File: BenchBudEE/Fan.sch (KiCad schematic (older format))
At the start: 11 parts, among them Q2 DMN65D8L-7, Q3 B130-13-F, Q4 B130-13-F, U10 MCP4801, U4 OPA4170

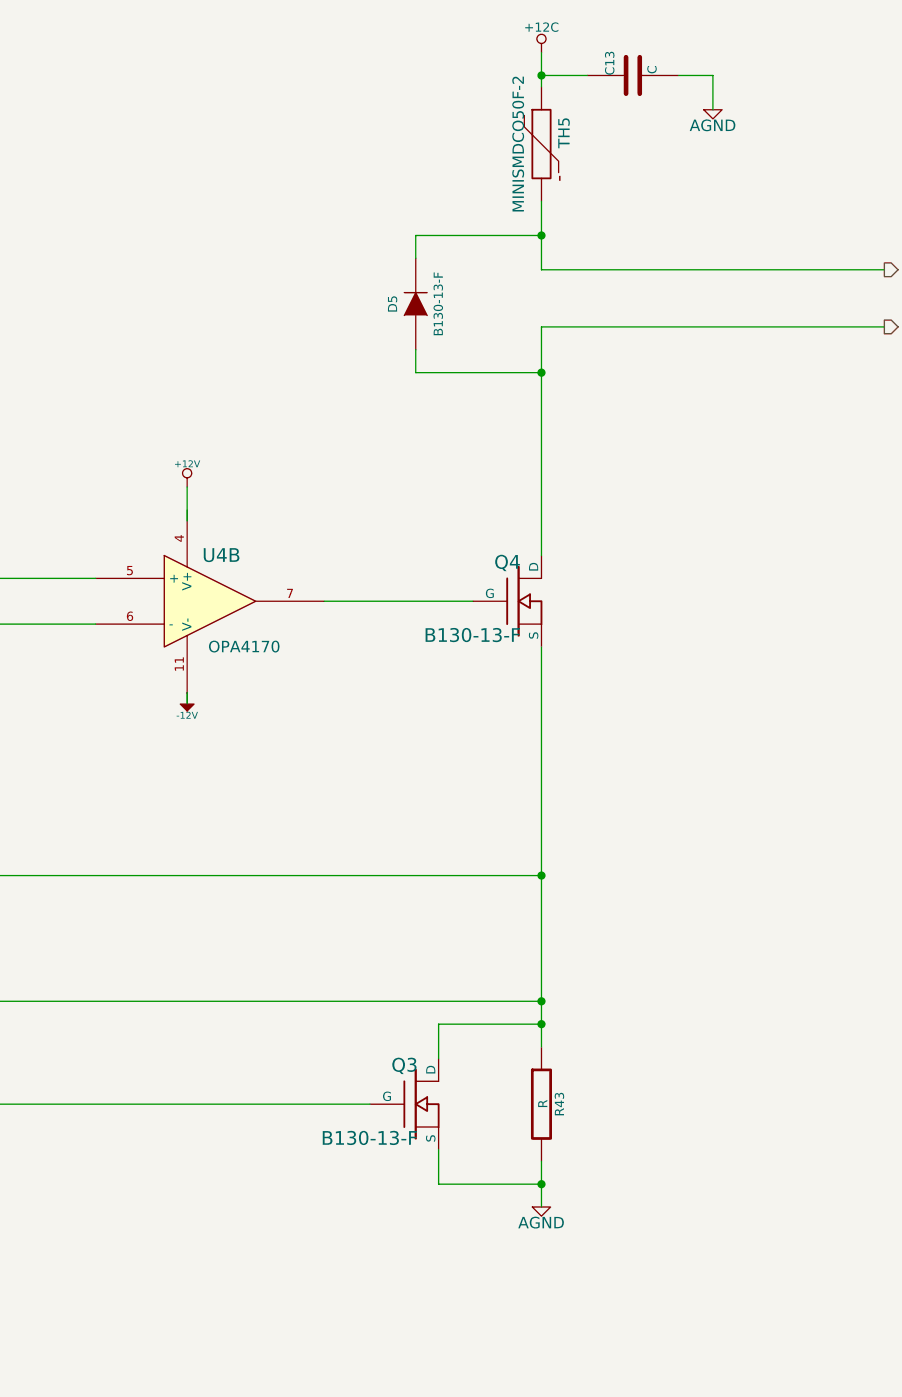
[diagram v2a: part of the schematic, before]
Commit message: Ground and Power Planes
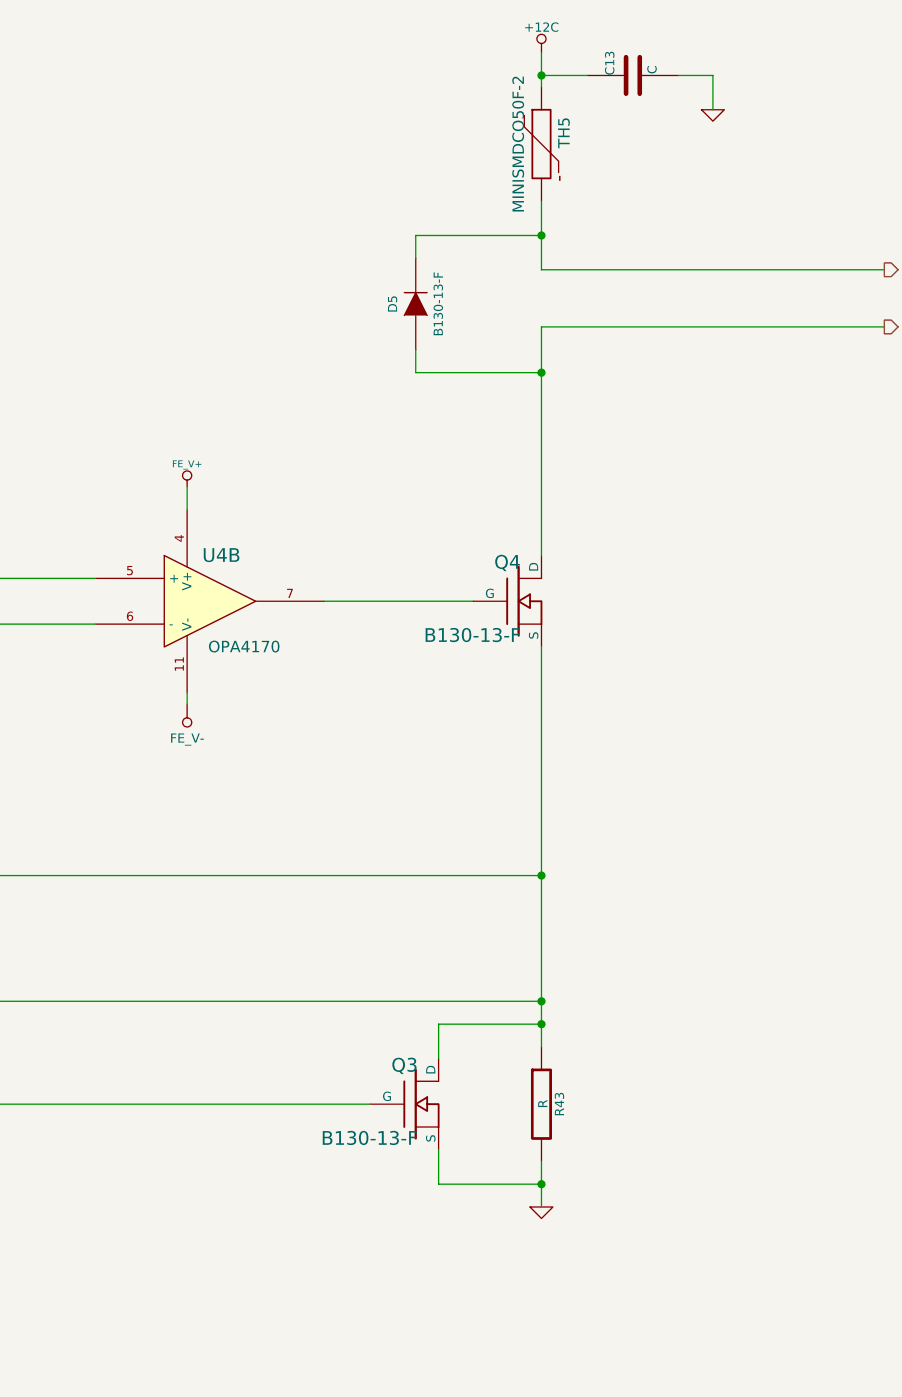
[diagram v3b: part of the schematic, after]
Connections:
- net labels added: FE_V+, FE_V-, GND
- net labels removed: +12V, -12V
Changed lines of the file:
@@
 Sheet 9 9
 Title ""
-Date "27 feb 2014"
+Date "1 mar 2014"
 Rev ""
 Comp ""
@@
 	1    0    0    -1
 $EndComp
-$Comp
-L AGND #PWR055
-U 1 1 52F13D75
-P 9100 5750
-F 0 "#PWR055" H 9100 5750 40  0001 C CNN
-F 1 "AGND" H 9100 5680 50  0000 C CNN
-F 2 "" H 9100 5750 60  0000 C CNN
-F 3 "" H 9100 5750 60  0000 C CNN
-	1    9100 5750
-	1    0    0    -1
-$EndComp
 Wire Wire Line
 	9100 5550 9100 5750
 Wire Wire Line
 	6100 3200 7150 3200
-$Comp
-L +12V #PWR056
-U 1 1 52F13D90
-P 7550 2600
-F 0 "#PWR056" H 7550 2550 20  0001 C CNN
-F 1 "+12V" H 7550 2700 30  0000 C CNN
-F 2 "" H 7550 2600 60  0000 C CNN
-F 3 "" H 7550 2600 60  0000 C CNN
-	1    7550 2600
-	1    0    0    -1
-$EndComp
-$Comp
-L -12V #PWR057
-U 1 1 52F13D98
-P 7550 3500
-F 0 "#PWR057" H 7550 3630 20  0001 C CNN
-F 1 "-12V" H 7550 3600 30  0000 C CNN
-F 2 "" H 7550 3500 60  0000 C CNN
-F 3 "" H 7550 3500 60  0000 C CNN
-	1    7550 3500
-	-1   0    0    1
-$EndComp
 Wire Wire Line
 	7550 3550 7550 3500
 Wire Wire Line
-	7550 2600 7550 2750
-Wire Wire Line
 	9100 1900 9100 2900
 Wire Wire Line
@@
 	5100 3750 5100 3900
 $Comp
-L AGND #PWR058
+L AGND #PWR61
 U 1 1 52F13E8F
 P 5100 3900
-F 0 "#PWR058" H 5100 3900 40  0001 C CNN
+F 0 "#PWR61" H 5100 3900 40  0001 C CNN
 F 1 "AGND" H 5100 3830 50  0000 C CNN
 F 2 "" H 5100 3900 60  0000 C CNN
@@
 FAN_MODE
 $Comp
-L +12C #PWR059
+L +12C #PWR64
 U 1 1 52FA7706
 P 9100 700
-F 0 "#PWR059" H 9100 670 30  0001 C CNN
+F 0 "#PWR64" H 9100 670 30  0001 C CNN
 F 1 "+12C" H 9100 810 40  0000 C CNN
 F 2 "" H 9100 700 60  0000 C CNN
@@
 $EndComp
 $Comp
-L +5V #PWR060
+L +5V #PWR59
 U 1 1 53092691
 P 2050 1900
-F 0 "#PWR060" H 2050 1990 20  0001 C CNN
+F 0 "#PWR59" H 2050 1990 20  0001 C CNN
 F 1 "+5V" H 2050 1990 30  0000 C CNN
 F 2 "" H 2050 1900 60  0000 C CNN
@@
 $EndComp
 $Comp
-L AGND #PWR061
+L AGND #PWR58
 U 1 1 53092697
 P 1350 2150
-F 0 "#PWR061" H 1350 2150 40  0001 C CNN
+F 0 "#PWR58" H 1350 2150 40  0001 C CNN
 F 1 "AGND" H 1350 2080 50  0000 C CNN
 F 2 "" H 1350 2150 60  0000 C CNN
@@
 	1350 2050 1350 2150
 $Comp
-L AGND #PWR062
+L AGND #PWR60
 U 1 1 530926A2
 P 2050 3850
-F 0 "#PWR062" H 2050 3850 40  0001 C CNN
+F 0 "#PWR60" H 2050 3850 40  0001 C CNN
 F 1 "AGND" H 2050 3780 50  0000 C CNN
 F 2 "" H 2050 3850 60  0000 C CNN
@@
 Wire Wire Line
 	9850 800  9850 950
-$Comp
-L AGND #PWR063
-U 1 1 53092F66
-P 9850 950
-F 0 "#PWR063" H 9850 950 40  0001 C CNN
-F 1 "AGND" H 9850 880 50  0000 C CNN
-F 2 "" H 9850 950 60  0000 C CNN
-F 3 "" H 9850 950 60  0000 C CNN
-	1    9850 950
-	1    0    0    -1
-$EndComp
 Connection ~ 9100 4300
 $Comp
@@
 	1    0    0    -1
 $EndComp
+$Comp
+L FE_V+ #PWR62
+U 1 1 5311A253
+P 7550 2600
+F 0 "#PWR62" H 7550 2700 30  0001 C CNN
+F 1 "FE_V+" H 7550 2700 30  0000 C CNN
+F 2 "" H 7550 2600 60  0000 C CNN
+F 3 "" H 7550 2600 60  0000 C CNN
+	1    7550 2600
+	1    0    0    -1
+$EndComp
+$Comp
+L FE_V- #PWR63
+U 1 1 5311A259
+P 7550 3550
+F 0 "#PWR63" H 7550 3750 40  0001 C CNN
+F 1 "FE_V-" H 7550 3700 40  0000 C CNN
+F 2 "~" H 7550 3550 60  0000 C CNN
+F 3 "~" H 7550 3550 60  0000 C CNN
+	1    7550 3550
+	-1   0    0    1
+$EndComp
+Wire Wire Line
+	7550 2700 7550 2600
+$Comp
+L GND #PWR65
+U 1 1 5311BFD1
+P 9100 5750
+F 0 "#PWR65" H 9100 5750 30  0001 C CNN
+F 1 "GND" H 9100 5680 30  0001 C CNN
+F 2 "" H 9100 5750 60  0000 C CNN
+F 3 "" H 9100 5750 60  0000 C CNN
+	1    9100 5750
+	1    0    0    -1
+$EndComp
+$Comp
+L GND #PWR66
+U 1 1 5311BFEA
+P 9850 950
+F 0 "#PWR66" H 9850 950 30  0001 C CNN
+F 1 "GND" H 9850 880 30  0001 C CNN
+F 2 "" H 9850 950 60  0000 C CNN
+F 3 "" H 9850 950 60  0000 C CNN
+	1    9850 950
+	1    0    0    -1
+$EndComp

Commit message: Layout Work Session 4
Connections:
- net GND is gone; now on net GND_FAN: C13.2, Q3.3 (S), R43.2
- net AGND renamed GND_FAN
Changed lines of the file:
@@
 Sheet 9 9
 Title ""
-Date "1 mar 2014"
+Date "2 mar 2014"
 Rev ""
 Comp ""
@@
 Wire Wire Line
 	5100 3750 5100 3900
-$Comp
-L AGND #PWR051
-U 1 1 52F13E8F
-P 5100 3900
-F 0 "#PWR051" H 5100 3900 40  0001 C CNN
-F 1 "AGND" H 5100 3830 50  0000 C CNN
-F 2 "" H 5100 3900 60  0000 C CNN
-F 3 "" H 5100 3900 60  0000 C CNN
-	1    5100 3900
-	1    0    0    -1
-$EndComp
 Text HLabel 1500 4850 0    60   Output ~ 0
 CURR_MEAS
@@
 FAN_MODE
 $Comp
-L +12C #PWR052
+L +12C #PWR050
 U 1 1 52FA7706
 P 9100 700
-F 0 "#PWR052" H 9100 670 30  0001 C CNN
+F 0 "#PWR050" H 9100 670 30  0001 C CNN
 F 1 "+12C" H 9100 810 40  0000 C CNN
 F 2 "" H 9100 700 60  0000 C CNN
@@
 $EndComp
 $Comp
-L +5V #PWR053
+L +5V #PWR051
 U 1 1 53092691
 P 2050 1900
-F 0 "#PWR053" H 2050 1990 20  0001 C CNN
+F 0 "#PWR051" H 2050 1990 20  0001 C CNN
 F 1 "+5V" H 2050 1990 30  0000 C CNN
 F 2 "" H 2050 1900 60  0000 C CNN
@@
 	1    0    0    -1
 $EndComp
-$Comp
-L AGND #PWR054
-U 1 1 53092697
-P 1350 2150
-F 0 "#PWR054" H 1350 2150 40  0001 C CNN
-F 1 "AGND" H 1350 2080 50  0000 C CNN
-F 2 "" H 1350 2150 60  0000 C CNN
-F 3 "" H 1350 2150 60  0000 C CNN
-	1    1350 2150
-	1    0    0    -1
-$EndComp
 Wire Wire Line
 	2050 1900 2050 2250
@@
 Wire Wire Line
 	1350 2050 1350 2150
-$Comp
-L AGND #PWR055
-U 1 1 530926A2
-P 2050 3850
-F 0 "#PWR055" H 2050 3850 40  0001 C CNN
-F 1 "AGND" H 2050 3780 50  0000 C CNN
-F 2 "" H 2050 3850 60  0000 C CNN
-F 3 "" H 2050 3850 60  0000 C CNN
-	1    2050 3850
-	1    0    0    -1
-$EndComp
 Wire Wire Line
 	2050 3750 2050 3850
@@
 $EndComp
 $Comp
-L FE_V+ #PWR056
+L FE_V+ #PWR052
 U 1 1 5311A253
 P 7550 2600
-F 0 "#PWR056" H 7550 2700 30  0001 C CNN
+F 0 "#PWR052" H 7550 2700 30  0001 C CNN
 F 1 "FE_V+" H 7550 2700 30  0000 C CNN
 F 2 "" H 7550 2600 60  0000 C CNN
@@
 	7550 2700 7550 2600
 $Comp
-L GND #PWR057
-U 1 1 5311BFD1
+L GND_FAN #PWR053
+U 1 1 5313100D
+P 9850 950
+F 0 "#PWR053" H 9850 950 30  0001 C CNN
+F 1 "GND_FAN" H 9850 880 30  0000 C CNN
+F 2 "" H 9850 950 60  0000 C CNN
+F 3 "" H 9850 950 60  0000 C CNN
+	1    9850 950
+	1    0    0    -1
+$EndComp
+$Comp
+L GND_FAN #PWR054
+U 1 1 5313102E
 P 9100 5750
-F 0 "#PWR057" H 9100 5750 30  0001 C CNN
-F 1 "GND" H 9100 5680 30  0001 C CNN
+F 0 "#PWR054" H 9100 5750 30  0001 C CNN
+F 1 "GND_FAN" H 9100 5680 30  0000 C CNN
 F 2 "" H 9100 5750 60  0000 C CNN
 F 3 "" H 9100 5750 60  0000 C CNN
@@
 $EndComp
 $Comp
-L GND #PWR058
-U 1 1 5311BFEA
-P 9850 950
-F 0 "#PWR058" H 9850 950 30  0001 C CNN
-F 1 "GND" H 9850 880 30  0001 C CNN
-F 2 "" H 9850 950 60  0000 C CNN
-F 3 "" H 9850 950 60  0000 C CNN
-	1    9850 950
-	1    0    0    -1
-$EndComp
+L GND_FAN #PWR055
+U 1 1 5313103E
+P 5100 3900
+F 0 "#PWR055" H 5100 3900 30  0001 C CNN
+F 1 "GND_FAN" H 5100 3830 30  0000 C CNN
+F 2 "" H 5100 3900 60  0000 C CNN
+F 3 "" H 5100 3900 60  0000 C CNN
+	1    5100 3900
+	1    0    0    -1
+$EndComp
+$Comp
+L GND_FAN #PWR056
+U 1 1 53131044
+P 2050 3850
+F 0 "#PWR056" H 2050 3850 30  0001 C CNN
+F 1 "GND_FAN" H 2050 3780 30  0000 C CNN
+F 2 "" H 2050 3850 60  0000 C CNN
+F 3 "" H 2050 3850 60  0000 C CNN
+	1    2050 3850
+	1    0    0    -1
+$EndComp
+$Comp
+L GND_FAN #PWR057
+U 1 1 5313104A
+P 1350 2150
+F 0 "#PWR057" H 1350 2150 30  0001 C CNN
+F 1 "GND_FAN" H 1350 2080 30  0000 C CNN
+F 2 "" H 1350 2150 60  0000 C CNN
+F 3 "" H 1350 2150 60  0000 C CNN
+	1    1350 2150
+	1    0    0    -1
+$EndComp

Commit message: Layout Work Session 5
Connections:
- net GND_FAN renamed AGND
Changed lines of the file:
@@
 FAN_MODE
 $Comp
-L +12C #PWR050
+L +12C #PWR051
 U 1 1 52FA7706
 P 9100 700
-F 0 "#PWR050" H 9100 670 30  0001 C CNN
+F 0 "#PWR051" H 9100 670 30  0001 C CNN
 F 1 "+12C" H 9100 810 40  0000 C CNN
 F 2 "" H 9100 700 60  0000 C CNN
@@
 $EndComp
 $Comp
-L +5V #PWR051
+L +5V #PWR052
 U 1 1 53092691
 P 2050 1900
-F 0 "#PWR051" H 2050 1990 20  0001 C CNN
+F 0 "#PWR052" H 2050 1990 20  0001 C CNN
 F 1 "+5V" H 2050 1990 30  0000 C CNN
 F 2 "" H 2050 1900 60  0000 C CNN
@@
 $EndComp
 $Comp
-L FE_V+ #PWR052
+L FE_V+ #PWR053
 U 1 1 5311A253
 P 7550 2600
-F 0 "#PWR052" H 7550 2700 30  0001 C CNN
+F 0 "#PWR053" H 7550 2700 30  0001 C CNN
 F 1 "FE_V+" H 7550 2700 30  0000 C CNN
 F 2 "" H 7550 2600 60  0000 C CNN
@@
 	7550 2700 7550 2600
 $Comp
-L GND_FAN #PWR053
-U 1 1 5313100D
-P 9850 950
-F 0 "#PWR053" H 9850 950 30  0001 C CNN
-F 1 "GND_FAN" H 9850 880 30  0000 C CNN
-F 2 "" H 9850 950 60  0000 C CNN
-F 3 "" H 9850 950 60  0000 C CNN
-	1    9850 950
+L AGND #PWR054
+U 1 1 5313633C
+P 5100 3900
+F 0 "#PWR054" H 5100 3900 40  0001 C CNN
+F 1 "AGND" H 5100 3830 50  0000 C CNN
+F 2 "" H 5100 3900 60  0000 C CNN
+F 3 "" H 5100 3900 60  0000 C CNN
+	1    5100 3900
 	1    0    0    -1
 $EndComp
 $Comp
-L GND_FAN #PWR054
-U 1 1 5313102E
+L AGND #PWR055
+U 1 1 53136358
 P 9100 5750
-F 0 "#PWR054" H 9100 5750 30  0001 C CNN
-F 1 "GND_FAN" H 9100 5680 30  0000 C CNN
+F 0 "#PWR055" H 9100 5750 40  0001 C CNN
+F 1 "AGND" H 9100 5680 50  0000 C CNN
 F 2 "" H 9100 5750 60  0000 C CNN
 F 3 "" H 9100 5750 60  0000 C CNN
@@
 $EndComp
 $Comp
-L GND_FAN #PWR055
-U 1 1 5313103E
-P 5100 3900
-F 0 "#PWR055" H 5100 3900 30  0001 C CNN
-F 1 "GND_FAN" H 5100 3830 30  0000 C CNN
-F 2 "" H 5100 3900 60  0000 C CNN
-F 3 "" H 5100 3900 60  0000 C CNN
-	1    5100 3900
-	1    0    0    -1
-$EndComp
-$Comp
-L GND_FAN #PWR056
-U 1 1 53131044
+L AGND #PWR056
+U 1 1 5313635E
 P 2050 3850
-F 0 "#PWR056" H 2050 3850 30  0001 C CNN
-F 1 "GND_FAN" H 2050 3780 30  0000 C CNN
+F 0 "#PWR056" H 2050 3850 40  0001 C CNN
+F 1 "AGND" H 2050 3780 50  0000 C CNN
 F 2 "" H 2050 3850 60  0000 C CNN
 F 3 "" H 2050 3850 60  0000 C CNN
@@
 $EndComp
 $Comp
-L GND_FAN #PWR057
-U 1 1 5313104A
+L AGND #PWR057
+U 1 1 53136374
 P 1350 2150
-F 0 "#PWR057" H 1350 2150 30  0001 C CNN
-F 1 "GND_FAN" H 1350 2080 30  0000 C CNN
+F 0 "#PWR057" H 1350 2150 40  0001 C CNN
+F 1 "AGND" H 1350 2080 50  0000 C CNN
 F 2 "" H 1350 2150 60  0000 C CNN
 F 3 "" H 1350 2150 60  0000 C CNN
@@
 	1    0    0    -1
 $EndComp
+$Comp
+L AGND #PWR058
+U 1 1 5313637A
+P 9850 950
+F 0 "#PWR058" H 9850 950 40  0001 C CNN
+F 1 "AGND" H 9850 880 50  0000 C CNN
+F 2 "" H 9850 950 60  0000 C CNN
+F 3 "" H 9850 950 60  0000 C CNN
+	1    9850 950
+	1    0    0    -1
+$EndComp
